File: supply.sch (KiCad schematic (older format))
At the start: 93 parts, among them IC12 74HC00PW, IC13 SN74LVC1G126DCKR, IC4 TPS7A0518PDBVT, J12 533980471, T3 BSS138APW, U1 LM3671MF-3.3/NOPB, U2 LM62440-Q1, U3 SN74LXC1T45DBVR, U5 LM3671MF-3.3/NOPB, U6 SIC477ED-T1-GE3

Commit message: Add LM3671MF-3.3/NOPB to library, change U1 and U5 library reference
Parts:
- U1, U5: symbol jetson-nano-baseboard:LM3671MF-1.5_NOPB -> jetson-nano-baseboard:LM3671MF-3.3_NOPB
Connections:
- net at U1.3 (EN): no longer R39.1
- net at U5.3 (EN): no longer R52.1
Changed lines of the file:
@@
 $EndComp
 $Comp
-L jetson-nano-baseboard:LM3671MF-1.5_NOPB U1
+L jetson-nano-baseboard:LM3671MF-3.3_NOPB U1
 U 1 1 61EC62D9
 P 2575 7925
@@
 $EndComp
 $Comp
-L jetson-nano-baseboard:LM3671MF-1.5_NOPB U5
+L jetson-nano-baseboard:LM3671MF-3.3_NOPB U5
 U 1 1 6217855E
 P 2575 8950

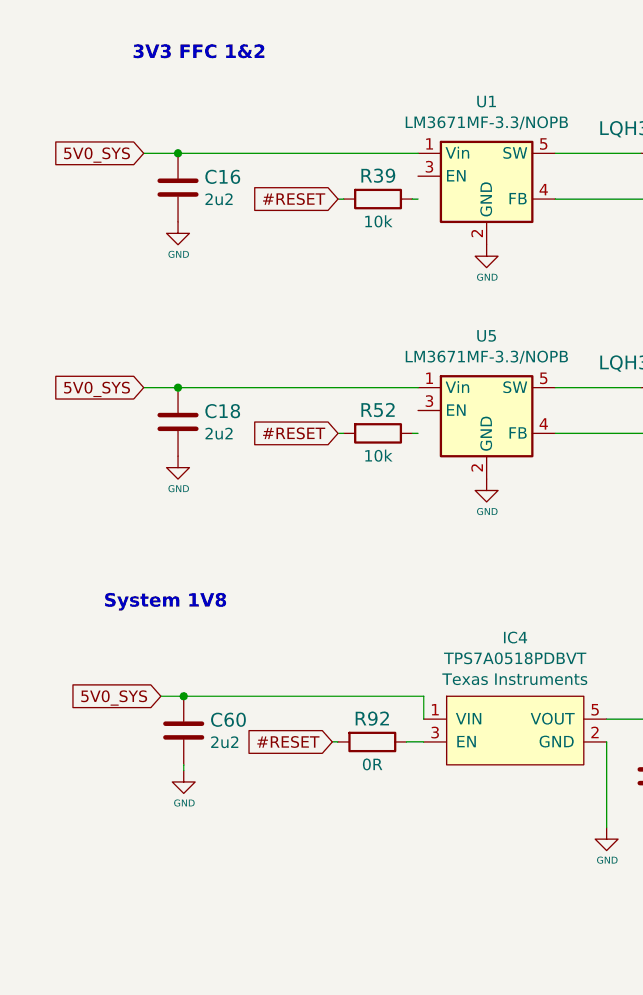
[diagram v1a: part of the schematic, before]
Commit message: Fix connections between resistors and DCDCs
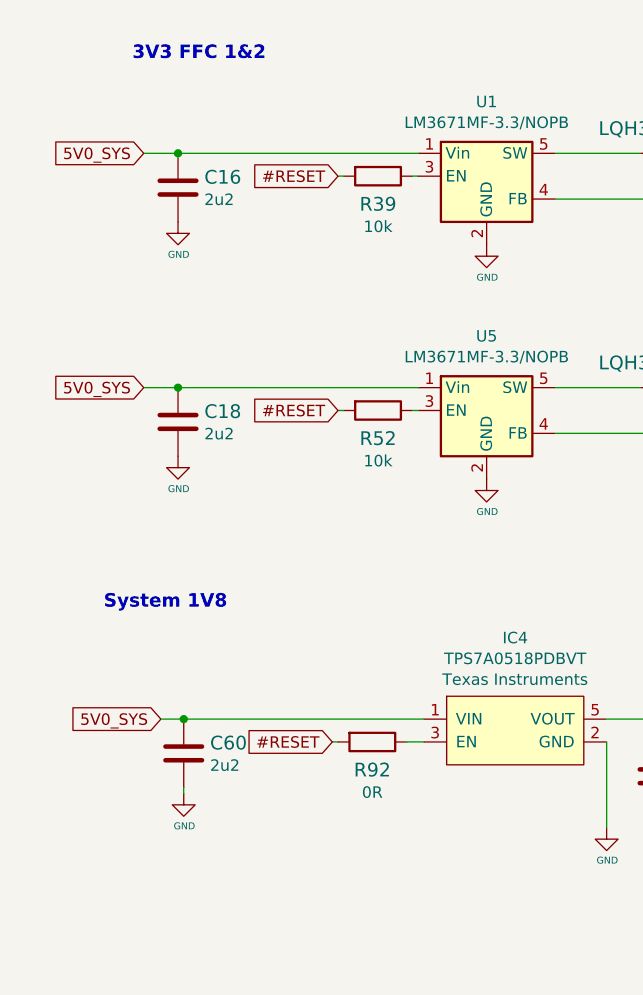
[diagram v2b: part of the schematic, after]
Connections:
- net at U1.3 (EN): now also R39.1
- net at U5.3 (EN): now also R52.1
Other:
- moved on the sheet: C60, R39, R52
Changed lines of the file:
@@
 Text Notes 900  9825 0    59   ~ 12
 System 1V8
-Text GLabel 1150 10200 0    50   Input ~ 0
+Text GLabel 1150 10300 0    50   Input ~ 0
 5V0_SYS
 Text GLabel 3325 10050 1    50   Input ~ 0
@@
 L jetson-nano-baseboard:GND #GND_064
 U 1 1 5E7103DD
-P 1250 10525
-F 0 "#GND_064" H 1250 10525 20  0001 C CNN
-F 1 "GND" H 1253 10382 30  0000 C CNN
-F 2 "" H 1250 10525 70  0001 C CNN
-F 3 "" H 1250 10525 70  0001 C CNN
-	1    1250 10525
+P 1250 10625
+F 0 "#GND_064" H 1250 10625 20  0001 C CNN
+F 1 "GND" H 1253 10482 30  0000 C CNN
+F 2 "" H 1250 10625 70  0001 C CNN
+F 3 "" H 1250 10625 70  0001 C CNN
+	1    1250 10625
 	1    0    0    -1
 $EndComp
@@
 	1900 10400 1925 10400
 Wire Wire Line
-	1250 10500 1250 10525
+	1250 10600 1250 10625
 Wire Wire Line
 	3325 10700 3325 10775
@@
 Wire Wire Line
 	2225 10400 2300 10400
-Wire Wire Line
-	2300 10200 2300 10300
 $Comp
 L jetson-nano-baseboard:TPS7A0518PDBVT IC4
@@
 $EndComp
 Wire Wire Line
-	1150 10200 1250 10200
+	1150 10300 1250 10300
 $Comp
 L jetson-nano-baseboard:C_2u2_0402 C60
 U 1 1 6173ABED
-P 1250 10350
-F 0 "C60" H 1365 10395 60  0000 L CNN
-F 1 "C_2u2_0402" H 1250 10200 60  0001 C CNN
-F 2 "jetson-nano-baseboard-footprints:0402-cap" H 1450 10550 60  0001 L CNN
-F 3 "" H 1250 10350 50  0001 C CNN
-F 4 "TDK" H 1450 10750 60  0001 L CNN "Manufacturer"
-F 5 "C1005X5R1A225K050BC" H 1450 10650 60  0001 L CNN "MPN"
-F 6 "2u2" H 1365 10297 50  0000 L CNN "Val"
-	1    1250 10350
-	1    0    0    -1
-$EndComp
-Connection ~ 1250 10200
-Wire Wire Line
-	1250 10200 2300 10200
+P 1250 10450
+F 0 "C60" H 1365 10495 60  0000 L CNN
+F 1 "C_2u2_0402" H 1250 10300 60  0001 C CNN
+F 2 "jetson-nano-baseboard-footprints:0402-cap" H 1450 10650 60  0001 L CNN
+F 3 "" H 1250 10450 50  0001 C CNN
+F 4 "TDK" H 1450 10850 60  0001 L CNN "Manufacturer"
+F 5 "C1005X5R1A225K050BC" H 1450 10750 60  0001 L CNN "MPN"
+F 6 "2u2" H 1365 10397 50  0000 L CNN "Val"
+	1    1250 10450
+	1    0    0    -1
+$EndComp
+Connection ~ 1250 10300
+Wire Wire Line
+	1250 10300 2300 10300
 $Comp
 L jetson-nano-baseboard:R_0R_0402 R92
 U 1 1 6173BBE4
 P 2075 10400
-F 0 "R92" H 2075 10300 60  0000 C CNN
+F 0 "R92" H 2075 10523 60  0000 C CNN
 F 1 "R_0R_0402" H 2075 10250 60  0001 C CNN
 F 2 "jetson-nano-baseboard-footprints:0402-res" H 2275 10600 60  0001 L CNN
@@
 F 4 "PANASONIC" H 2275 10800 60  0001 L CNN "Manufacturer"
 F 5 "ERJ2GE0R00X" H 2275 10700 60  0001 L CNN "MPN"
-F 6 "0R" H 2075 10500 50  0000 C CNN "Val"
+F 6 "0R" H 2075 10621 50  0000 C CNN "Val"
 	1    2075 10400
 	-1   0    0    1
@@
 	1    0    0    -1
 $EndComp
-Text GLabel 1925 8025 0    50   Input ~ 0
+Text GLabel 1925 7925 0    50   Input ~ 0
 #RESET
 $Comp
 L jetson-nano-baseboard:R_10k_0402 R39
 U 1 1 61FD0846
-P 2100 8025
-F 0 "R39" H 2100 7925 60  0000 C CNN
-F 1 "R_10k_0402" H 2100 7875 60  0001 C CNN
-F 2 "jetson-nano-baseboard-footprints:0402-res" H 2300 8225 60  0001 L CNN
-F 3 "" H 2100 8025 50  0001 C CNN
-F 4 "VISHAY" H 2300 8425 60  0001 L CNN "Manufacturer"
-F 5 "CRCW040210K0FKEDHP" H 2300 8325 60  0001 L CNN "MPN"
-F 6 "10k" H 2100 8125 50  0000 C CNN "Val"
-	1    2100 8025
+P 2100 7925
+F 0 "R39" H 2100 8048 60  0000 C CNN
+F 1 "R_10k_0402" H 2100 7775 60  0001 C CNN
+F 2 "jetson-nano-baseboard-footprints:0402-res" H 2300 8125 60  0001 L CNN
+F 3 "" H 2100 7925 50  0001 C CNN
+F 4 "VISHAY" H 2300 8325 60  0001 L CNN "Manufacturer"
+F 5 "CRCW040210K0FKEDHP" H 2300 8225 60  0001 L CNN "MPN"
+F 6 "10k" H 2100 8146 50  0000 C CNN "Val"
+	1    2100 7925
 	-1   0    0    1
 $EndComp
 Wire Wire Line
-	1925 8025 1950 8025
-Wire Wire Line
-	2275 8025 2250 8025
+	1925 7925 1950 7925
+Wire Wire Line
+	2275 7925 2250 7925
 Text GLabel 1075 7825 0    50   Input ~ 0
 5V0_SYS
@@
 	1    0    0    -1
 $EndComp
-Text GLabel 1925 9050 0    50   Input ~ 0
+Text GLabel 1925 8950 0    50   Input ~ 0
 #RESET
 $Comp
 L jetson-nano-baseboard:R_10k_0402 R52
 U 1 1 62178594
-P 2100 9050
-F 0 "R52" H 2100 8950 60  0000 C CNN
-F 1 "R_10k_0402" H 2100 8900 60  0001 C CNN
-F 2 "jetson-nano-baseboard-footprints:0402-res" H 2300 9250 60  0001 L CNN
-F 3 "" H 2100 9050 50  0001 C CNN
-F 4 "VISHAY" H 2300 9450 60  0001 L CNN "Manufacturer"
-F 5 "CRCW040210K0FKEDHP" H 2300 9350 60  0001 L CNN "MPN"
-F 6 "10k" H 2100 9150 50  0000 C CNN "Val"
-	1    2100 9050
+P 2100 8950
+F 0 "R52" H 2100 9073 60  0000 C CNN
+F 1 "R_10k_0402" H 2100 8800 60  0001 C CNN
+F 2 "jetson-nano-baseboard-footprints:0402-res" H 2300 9150 60  0001 L CNN
+F 3 "" H 2100 8950 50  0001 C CNN
+F 4 "VISHAY" H 2300 9350 60  0001 L CNN "Manufacturer"
+F 5 "CRCW040210K0FKEDHP" H 2300 9250 60  0001 L CNN "MPN"
+F 6 "10k" H 2100 9171 50  0000 C CNN "Val"
+	1    2100 8950
 	-1   0    0    1
 $EndComp
 Wire Wire Line
-	1925 9050 1950 9050
-Wire Wire Line
-	2275 9050 2250 9050
+	1925 8950 1950 8950
+Wire Wire Line
+	2275 8950 2250 8950
 Text GLabel 1075 8850 0    50   Input ~ 0
 5V0_SYS
